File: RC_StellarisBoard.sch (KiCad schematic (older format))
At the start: 68 parts, among them K1 CONN_3, K2 CONN_3, K3 CONN_3, K4 CONN_3, K5 CONN_3, P1 CONN_2, P10 XT-60 out, P11 CONN_1, P12 CONN_1, P2 CONN_1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

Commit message: v1 completa
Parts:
- removed P1: CONN_2, symbol CONN_2
- removed P8: I2C, symbol CONN_2
- added K6: CONN_3, symbol CONN_3
- added R26, R27: ina0, symbol R
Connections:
- net +3.3V: now also K6.3 (P3)
- net GND: now also R27.1, R27.2
- net SCL: now also K6.1 (P1)
- net SDA: now also K6.2 (PM)
- net ina_alert: now also R26.2; no longer P12.1
- new net: P12.1, R26.1

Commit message: added nordic
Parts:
- added P1, P14: CONN_4, symbol CONN_4
- added P13: CONN_1, symbol CONN_1
- added P8: CONN_3X2, symbol CONN_3X2
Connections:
- net +3.3V: now also P13.1, P14.1 (P1)
- net GND: now also P1.1 (P1)
- new net MISO: P1.4 (P4), P8.5
- new net MOSI: P14.3 (P3), P8.6
- new net SCK: P1.3 (P3), P8.3
- new net ~CE: P1.2 (P2), P8.2
- new net ~CS: P14.2 (P2), P8.4
- new net ~IRQ: P14.4 (P4), P8.1

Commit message: v3, n confirmado, added fan diode
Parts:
- added D3: DIODESCH, ~, symbol DIODESCH
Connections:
- net Battery_out: now also D3.2 (K)
- net at K5.1 (P1), Q3.D: now also D3.1 (A)

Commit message: corrigido erro buck boost
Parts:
- added C13: 22uF, ~, symbol C
- added R28: 0, symbol R
- R27: value ina0 -> 0
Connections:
- net +3.3V: now also C13.1, R28.1, R28.2; no longer U3.11 (VSEL)
- net +5V: now also U3.11 (VSEL)
- net GND: now also C13.2

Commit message: corrigido erro buck boost 1
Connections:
- net +5V: now also U3.6 (EN)

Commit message: valores
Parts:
- added R?: 22K, ~, symbol R
- C12: value 0.1uF -> 0.01uF
- C7: value 22uF -> 4u7
- R1, R11, R3, R5, R7: value R -> 100R
- R10: value R -> 4k7
- R19: value shunt -> R0015
- R2, R4, R6, R8: value R -> 0
- R24, R25: value 10k -> 10R
- R26: value ina0 -> 0
- R9: value R -> 22k
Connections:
- net +24V: now also R?.2
- net at D1.1 (A), Q4.G, R11.1: now also R?.1
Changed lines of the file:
@@
 P 1350 1000
 F 0 "R1" V 1430 1000 40  0000 C CNN
-F 1 "R" V 1357 1001 40  0000 C CNN
+F 1 "100R" V 1357 1001 40  0000 C CNN
 F 2 "~" V 1280 1000 30  0000 C CNN
 F 3 "~" H 1350 1000 30  0000 C CNN
@@
 P 1500 1000
 F 0 "R2" V 1580 1000 40  0000 C CNN
-F 1 "R" V 1507 1001 40  0000 C CNN
+F 1 "0" V 1507 1001 40  0000 C CNN
 F 2 "~" V 1430 1000 30  0000 C CNN
 F 3 "~" H 1500 1000 30  0000 C CNN
@@
 P 2150 1000
 F 0 "R3" V 2230 1000 40  0000 C CNN
-F 1 "R" V 2157 1001 40  0000 C CNN
+F 1 "100R" V 2157 1001 40  0000 C CNN
 F 2 "~" V 2080 1000 30  0000 C CNN
 F 3 "~" H 2150 1000 30  0000 C CNN
@@
 P 2300 1000
 F 0 "R4" V 2380 1000 40  0000 C CNN
-F 1 "R" V 2307 1001 40  0000 C CNN
+F 1 "0" V 2307 1001 40  0000 C CNN
 F 2 "~" V 2230 1000 30  0000 C CNN
 F 3 "~" H 2300 1000 30  0000 C CNN
@@
 P 2900 1000
 F 0 "R5" V 2980 1000 40  0000 C CNN
-F 1 "R" V 2907 1001 40  0000 C CNN
+F 1 "100R" V 2907 1001 40  0000 C CNN
 F 2 "~" V 2830 1000 30  0000 C CNN
 F 3 "~" H 2900 1000 30  0000 C CNN
@@
 P 3050 1000
 F 0 "R6" V 3130 1000 40  0000 C CNN
-F 1 "R" V 3057 1001 40  0000 C CNN
+F 1 "0" V 3057 1001 40  0000 C CNN
 F 2 "~" V 2980 1000 30  0000 C CNN
 F 3 "~" H 3050 1000 30  0000 C CNN
@@
 P 3600 1000
 F 0 "R7" V 3680 1000 40  0000 C CNN
-F 1 "R" V 3607 1001 40  0000 C CNN
+F 1 "100R" V 3607 1001 40  0000 C CNN
 F 2 "~" V 3530 1000 30  0000 C CNN
 F 3 "~" H 3600 1000 30  0000 C CNN
@@
 P 3750 1000
 F 0 "R8" V 3830 1000 40  0000 C CNN
-F 1 "R" V 3757 1001 40  0000 C CNN
+F 1 "0" V 3757 1001 40  0000 C CNN
 F 2 "~" V 3680 1000 30  0000 C CNN
 F 3 "~" H 3750 1000 30  0000 C CNN
@@
 P 2900 2900
 F 0 "R9" V 2980 2900 40  0000 C CNN
-F 1 "R" V 2907 2901 40  0000 C CNN
+F 1 "22k" V 2907 2901 40  0000 C CNN
 F 2 "~" V 2830 2900 30  0000 C CNN
 F 3 "~" H 2900 2900 30  0000 C CNN
@@
 P 2100 3400
 F 0 "R11" V 2180 3400 40  0000 C CNN
-F 1 "R" V 2107 3401 40  0000 C CNN
+F 1 "100R" V 2107 3401 40  0000 C CNN
 F 2 "~" V 2030 3400 30  0000 C CNN
 F 3 "~" H 2100 3400 30  0000 C CNN
@@
 P 2100 3850
 F 0 "R10" V 2180 3850 40  0000 C CNN
-F 1 "R" V 2107 3851 40  0000 C CNN
+F 1 "4k7" V 2107 3851 40  0000 C CNN
 F 2 "~" V 2030 3850 30  0000 C CNN
 F 3 "~" H 2100 3850 30  0000 C CNN
@@
 P 1350 2600
 F 0 "R19" V 1430 2600 40  0000 C CNN
-F 1 "shunt" V 1357 2601 40  0000 C CNN
+F 1 "R0015" V 1357 2601 40  0000 C CNN
 F 2 "" V 1280 2600 30  0000 C CNN
 F 3 "" H 1350 2600 30  0000 C CNN
@@
 P 8450 5950
 F 0 "C7" H 8450 6050 40  0000 L CNN
-F 1 "22uF" H 8456 5865 40  0000 L CNN
+F 1 "4u7" H 8456 5865 40  0000 L CNN
 F 2 "~" H 8488 5800 30  0000 C CNN
 F 3 "~" H 8450 5950 60  0000 C CNN
@@
 P 6950 2000
 F 0 "C12" H 6950 2100 40  0000 L CNN
-F 1 "0.1uF" H 6956 1915 40  0000 L CNN
+F 1 "0.01uF" H 6956 1915 40  0000 L CNN
 F 2 "~" H 6988 1850 30  0000 C CNN
 F 3 "~" H 6950 2000 60  0000 C CNN
@@
 P 6700 2200
 F 0 "R25" V 6780 2200 40  0000 C CNN
-F 1 "10k" V 6707 2201 40  0000 C CNN
+F 1 "10R" V 6707 2201 40  0000 C CNN
 F 2 "~" V 6630 2200 30  0000 C CNN
 F 3 "~" H 6700 2200 30  0000 C CNN
@@
 P 6700 1800
 F 0 "R24" V 6780 1800 40  0000 C CNN
-F 1 "10k" V 6707 1801 40  0000 C CNN
+F 1 "10R" V 6707 1801 40  0000 C CNN
 F 2 "~" V 6630 1800 30  0000 C CNN
 F 3 "~" H 6700 1800 30  0000 C CNN
@@
 P 1200 2200
 F 0 "R26" V 1280 2200 40  0000 C CNN
-F 1 "ina0" V 1207 2201 40  0000 C CNN
+F 1 "0" V 1207 2201 40  0000 C CNN
 F 2 "" V 1130 2200 30  0000 C CNN
 F 3 "" H 1200 2200 30  0000 C CNN
@@
 Connection ~ 7200 3150
 Wire Wire Line
-	2300 2800 2300 2750
-Wire Wire Line
-	2300 2750 1750 2750
+	2300 2750 2300 2800
+Wire Wire Line
+	1550 2750 2300 2750
 Connection ~ 2300 2750
 Wire Wire Line
-	1750 3150 1900 3150
+	1650 3150 1900 3150
 Wire Wire Line
 	1900 3150 1900 3000
@@
 	0    -1   -1   0
 $EndComp
+$Comp
+L R R?
+U 1 1 52D1A1F3
+P 1550 3000
+F 0 "R?" V 1630 3000 40  0000 C CNN
+F 1 "22K" V 1557 3001 40  0000 C CNN
+F 2 "~" V 1480 3000 30  0000 C CNN
+F 3 "~" H 1550 3000 30  0000 C CNN
+	1    1550 3000
+	-1   0    0    1
+$EndComp
+Connection ~ 1750 2750
+Wire Wire Line
+	1550 3250 1650 3250
+Wire Wire Line
+	1650 3250 1650 3150
 $EndSCHEMATC

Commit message: valores
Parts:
- R26: value 0 -> 0R
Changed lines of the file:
@@
 P 1200 2200
 F 0 "R26" V 1280 2200 40  0000 C CNN
-F 1 "0" V 1207 2201 40  0000 C CNN
+F 1 "0R" V 1207 2201 40  0000 C CNN
 F 2 "" V 1130 2200 30  0000 C CNN
 F 3 "" H 1200 2200 30  0000 C CNN

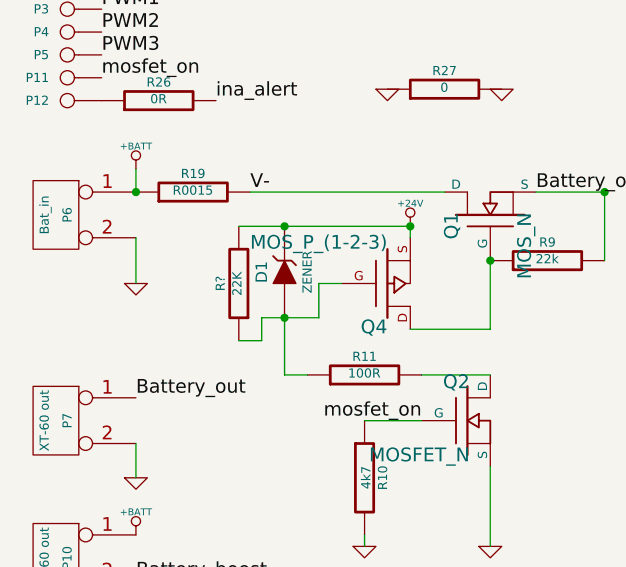
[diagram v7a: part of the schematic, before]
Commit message: resist mosfet P done
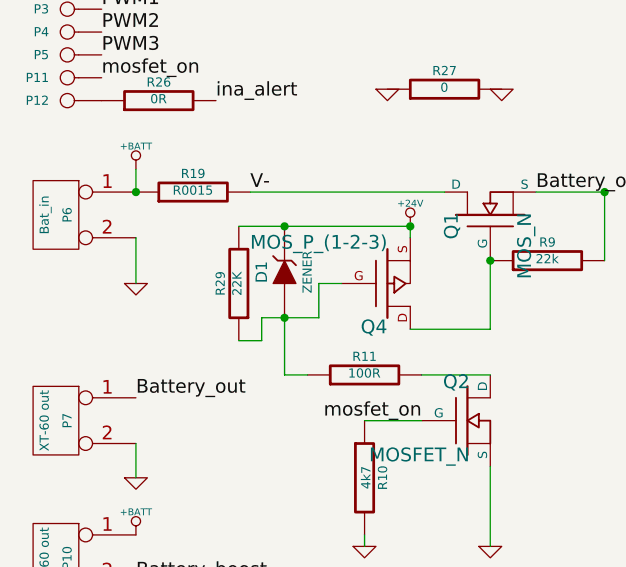
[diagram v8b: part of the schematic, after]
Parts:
- gave numbers to parts that had none: 1
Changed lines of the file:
@@
 $EndComp
 $Comp
-L R R?
+L R R29
 U 1 1 52D1A1F3
 P 1550 3000
-F 0 "R?" V 1630 3000 40  0000 C CNN
+F 0 "R29" V 1630 3000 40  0000 C CNN
 F 1 "22K" V 1557 3001 40  0000 C CNN
 F 2 "~" V 1480 3000 30  0000 C CNN
